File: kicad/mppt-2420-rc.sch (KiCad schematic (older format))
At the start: 10 parts, among them J1 MKDS 5/ 2-9,5, J2 MKDS 5/ 2-9,5, J5 Phoenix Contact MC 1,5

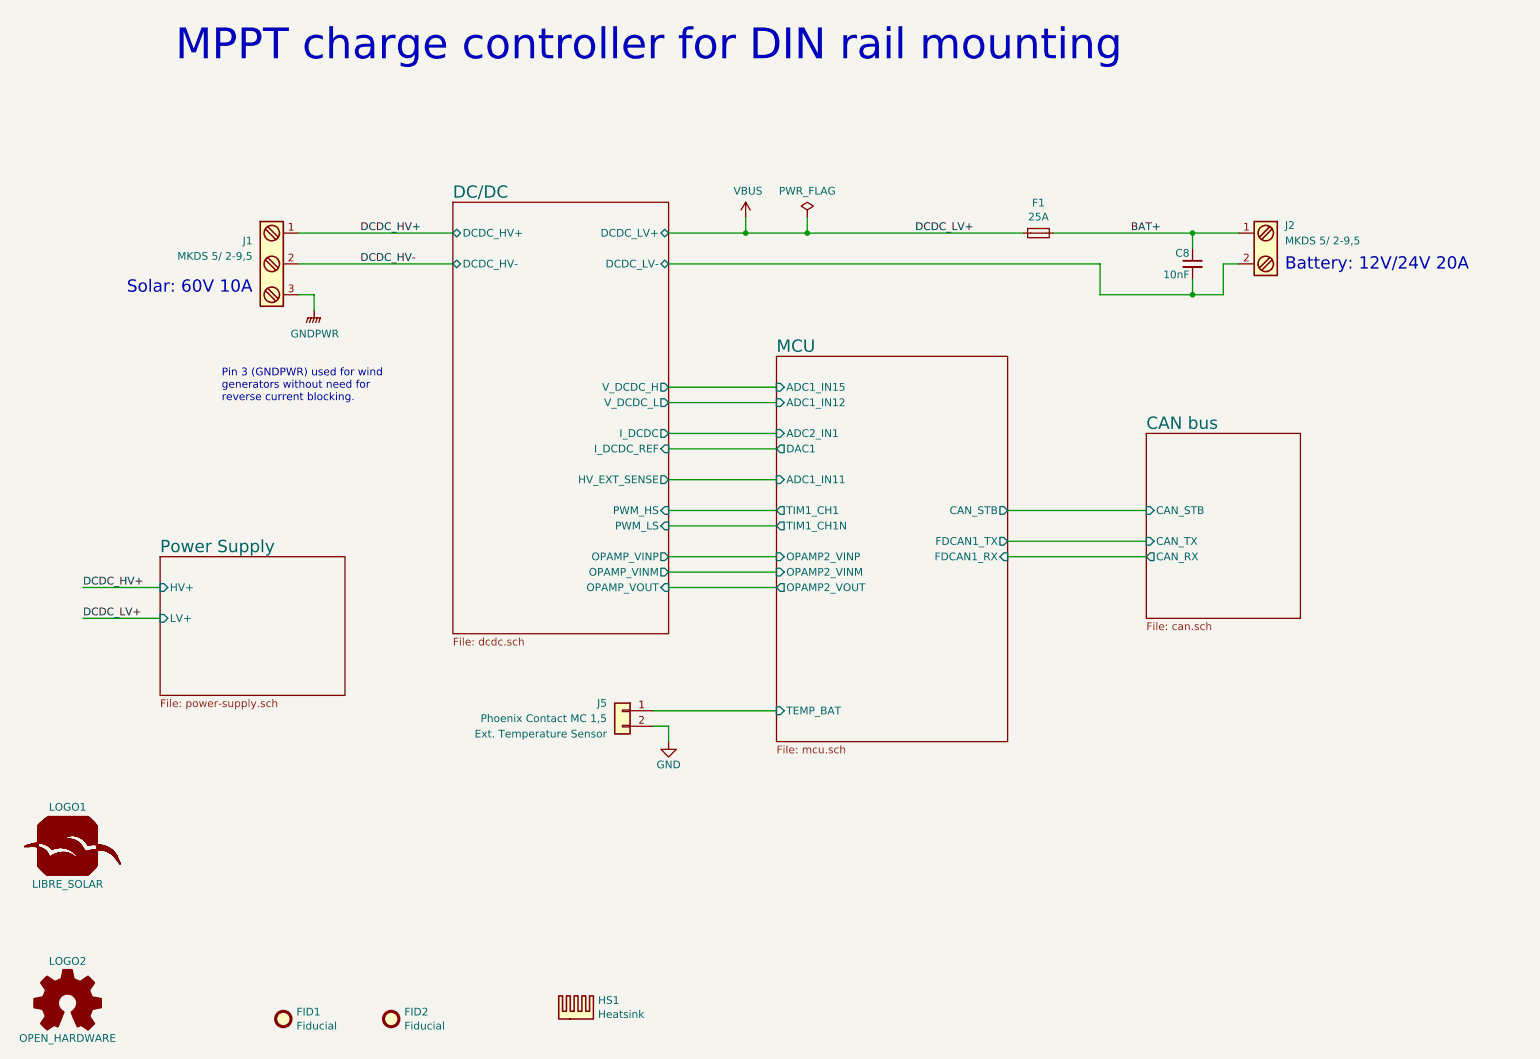
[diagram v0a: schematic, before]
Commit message: Fix errors after first prototype build-up
- Collision of capacitors with MOSFET clamps
- BOOT0 pin tied to GND
- Assignment of a few previously unasigned passives
- Add optional debug serial connector
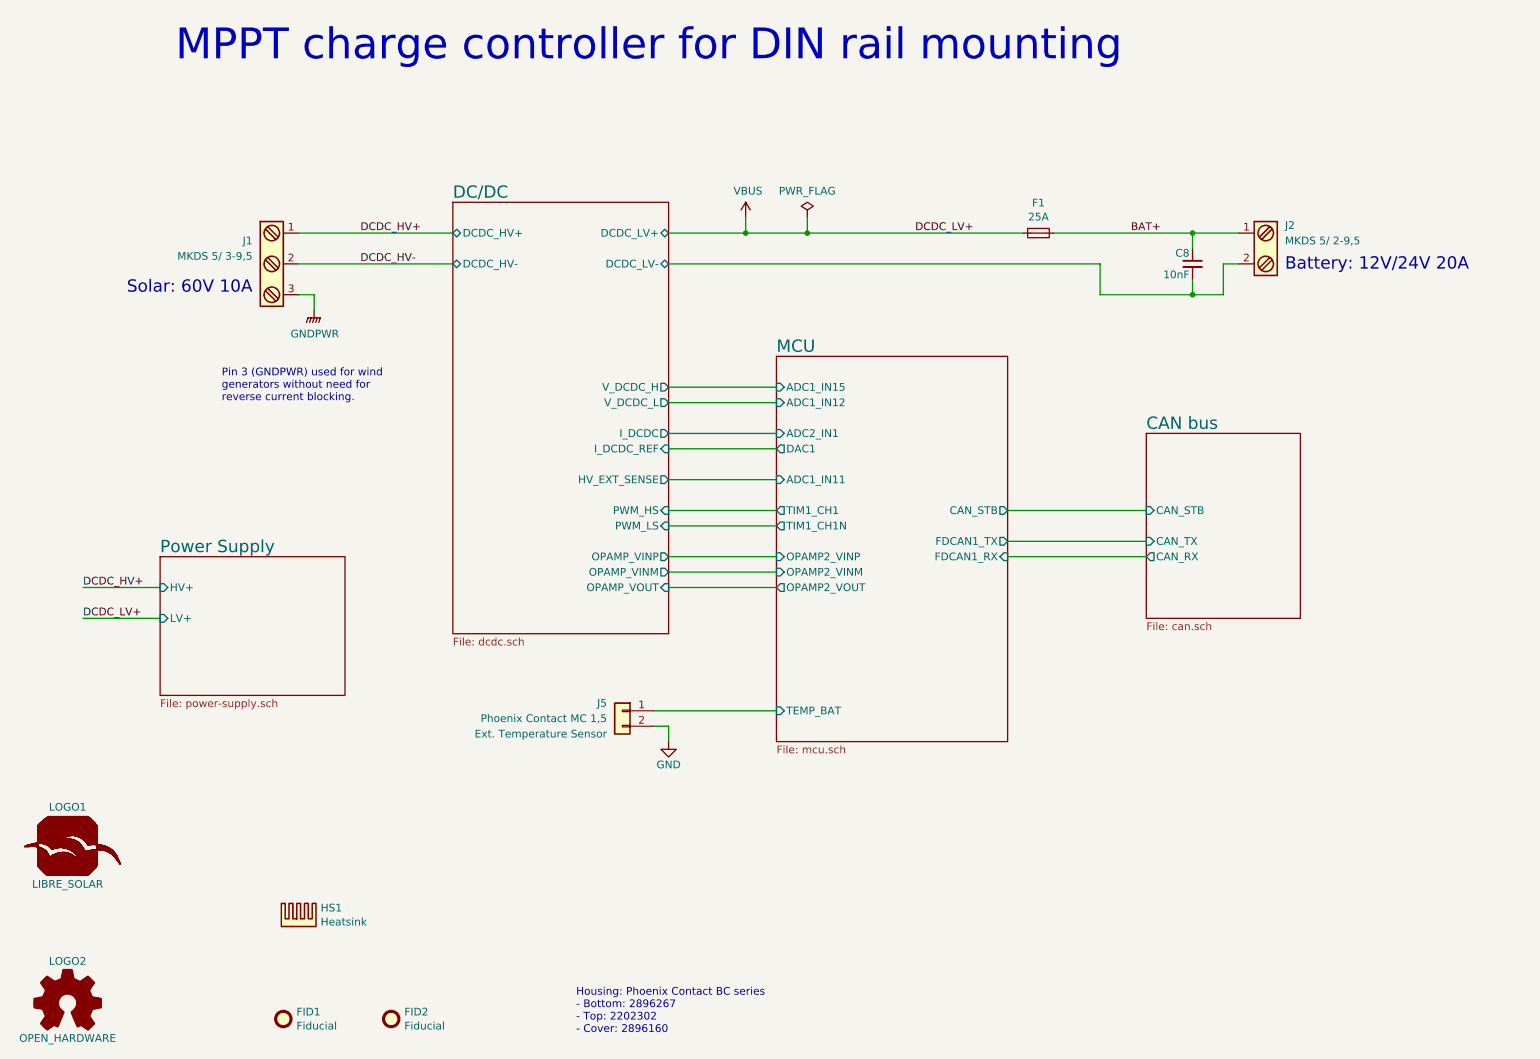
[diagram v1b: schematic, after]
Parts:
- HS1: Manufacturer (none) -> Fischer Elektronik; PartNumber (none) -> SK573-37,5
- J1: value MKDS 5/ 2-9,5 -> MKDS 5/ 3-9,5; Manufacturer (none) -> Phoenix Contact; PartNumber (none) -> 1714984
- J2: Manufacturer (none) -> Phoenix Contact; PartNumber (none) -> 1714971
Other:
- note added: "Housing: Phoenix Contact BC series\n- Bottom: 2896267\n- Top: 2202302\n- Cover: 2896160"
- moved on the sheet: HS1
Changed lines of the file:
@@
 Sheet 1 5
 Title "MPPT 2420 RC"
-Date "2020-02-20"
-Rev "0.1"
+Date "2020-05-30"
+Rev "0.1.1"
 Comp "Libre Solar Technologies GmbH"
 Comment1 "Author: Martin Jäger"
@@
 AR Path="/5CC2E802" Ref="J1"  Part="1"
 F 0 "J1" H 2600 2550 50  0000 R CNN
-F 1 "MKDS 5/ 2-9,5" H 2600 2450 50  0000 R CNN
+F 1 "MKDS 5/ 3-9,5" H 2600 2450 50  0000 R CNN
 F 2 "LibreSolar:Phoenix_Contact_MKDS_5-3-9,5" H 2700 2175 50  0001 C CNN
 F 3 "" H 2675 2400 50  0001 C CNN
+F 4 "Phoenix Contact" H 2700 2400 50  0001 C CNN "Manufacturer"
+F 5 "1714984" H 2700 2400 50  0001 C CNN "PartNumber"
 	1    2700 2400
 	1    0    0    -1
@@
 F 2 "LibreSolar:Phoenix_Contact_MKDS_5-2-9,5" H 9200 2075 50  0001 C CNN
 F 3 "" H 9175 2300 50  0001 C CNN
+F 4 "Phoenix Contact" H 9200 2300 50  0001 C CNN "Manufacturer"
+F 5 "1714971" H 9200 2300 50  0001 C CNN "PartNumber"
 	1    9200 2300
 	-1   0    0    -1
@@
 L Mechanical:Heatsink HS1
 U 1 1 5E1B0EED
-P 4700 7300
-F 0 "HS1" H 4842 7421 50  0000 L CNN
-F 1 "Heatsink" H 4842 7330 50  0000 L CNN
-F 2 "LibreSolar:Fischer_Elektronik_SK573_37,5" H 4712 7300 50  0001 C CNN
-F 3 "~" H 4712 7300 50  0001 C CNN
-	1    4700 7300
+P 2900 6700
+F 0 "HS1" H 3042 6821 50  0000 L CNN
+F 1 "Heatsink" H 3042 6730 50  0000 L CNN
+F 2 "LibreSolar:Fischer_Elektronik_SK573_37,5" H 2912 6700 50  0001 C CNN
+F 3 "~" H 2912 6700 50  0001 C CNN
+F 4 "Fischer Elektronik" H 2900 6700 50  0001 C CNN "Manufacturer"
+F 5 "SK573-37,5" H 2900 6700 50  0001 C CNN "PartNumber"
+	1    2900 6700
 	1    0    0    -1
 $EndComp
@@
 Text Notes 2400 3300 0    50   ~ 0
 Pin 3 (GNDPWR) used for wind\ngenerators without need for \nreverse current blocking.
+Text Notes 4700 7400 0    50   ~ 0
+Housing: Phoenix Contact BC series\n- Bottom: 2896267\n- Top: 2202302\n- Cover: 2896160
 $EndSCHEMATC

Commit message: Fix some references and part numbers
See issues #3, #5, #7, #8 and #9.
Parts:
- added XF1: ATO blade fuse, LibreSolar:Keystone-Fuse-3557-2, symbol LibreSolar:Fuse_Holder
- C8: Manufacturer (none) -> Murata; PartNumber (none) -> GCM188R72A103KA37D; Remarks 50V, X7R -> 100V, X7R
- F1: footprint LibreSolar:Keystone-Fuse-3557-2 -> LibreSolar:NULL; symbol LibreSolar:Fuse -> LibreSolar:Fuse_PlugIn; Manufacturer (none) -> Littelfuse; PartNumber (none) -> 0287025.PXCN
- HS1: Remarks (none) -> 3x MOSFET clips THFU 2 and thermal interface material needed
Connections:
- net BAT+: now also XF1.2; no longer F1.2
- net VBUS: now also XF1.1; no longer F1.1
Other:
- note added: "10k NTC thermistor\n\nMatching connector: \nPhoenix Contact 1745894"
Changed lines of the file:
@@
 F 2 "LibreSolar:C_0603_1608" H 8700 2400 50  0001 C CNN
 F 3 "" H 8700 2400 50  0000 C CNN
-F 4 "" H 6600 650 50  0001 C CNN "Manufacturer"
-F 5 "" H 6600 650 50  0001 C CNN "PartNumber"
-F 6 "50V, X7R" H 6100 300 60  0001 C CNN "Remarks"
+F 4 "Murata" H 6600 650 50  0001 C CNN "Manufacturer"
+F 5 "GCM188R72A103KA37D" H 6600 650 50  0001 C CNN "PartNumber"
+F 6 "100V, X7R" H 6100 300 60  0001 C CNN "Remarks"
 	1    8700 2400
 	-1   0    0    -1
@@
 	9000 2200 8700 2200
 $Comp
-L LibreSolar:Fuse F?
+L LibreSolar:Fuse_PlugIn F?
 U 1 1 5DADB2CD
-P 7700 2200
+P 7700 2100
 AR Path="/5C5B93EE/5DADB2CD" Ref="F?"  Part="1"
 AR Path="/5DADB2CD" Ref="F1"  Part="1"
-F 0 "F1" H 7700 2396 50  0000 C CNN
-F 1 "25A" H 7700 2305 50  0000 C CNN
-F 2 "LibreSolar:Keystone-Fuse-3557-2" H 7700 2200 50  0001 C CNN
-F 3 "" H 7700 2200 50  0000 C CNN
-	1    7700 2200
-	1    0    0    -1
-$EndComp
-Wire Wire Line
-	7800 2200 8700 2200
+F 0 "F1" H 7550 2200 50  0000 C CNN
+F 1 "25A" H 7850 2200 50  0000 C CNN
+F 2 "LibreSolar:NULL" H 7700 2100 50  0001 C CNN
+F 3 "" H 7700 2100 50  0001 C CNN
+F 4 "Littelfuse" H 7700 2100 50  0001 C CNN "Manufacturer"
+F 5 "0287025.PXCN" H 7700 2100 50  0001 C CNN "PartNumber"
+F 6 "" H 7700 2100 50  0001 C CNN "Config"
+	1    7700 2100
+	1    0    0    -1
+$EndComp
 Wire Wire Line
 	5300 2200 5800 2200
@@
 F 4 "Fischer Elektronik" H 2900 6700 50  0001 C CNN "Manufacturer"
 F 5 "SK573-37,5" H 2900 6700 50  0001 C CNN "PartNumber"
+F 6 "3x MOSFET clips THFU 2 and thermal interface material needed" H 2900 6700 50  0001 C CNN "Remarks"
 	1    2900 6700
 	1    0    0    -1
@@
 	2900 2200 3900 2200
 Wire Wire Line
-	6200 2200 7600 2200
+	6200 2200 7500 2200
 Wire Wire Line
 	2900 2600 3000 2600
@@
 	3000 2600 3000 2700
 Wire Wire Line
-	5300 2400 8100 2400
-Wire Wire Line
-	8100 2400 8100 2600
-Wire Wire Line
-	8100 2600 8700 2600
+	5300 2400 7200 2400
+Wire Wire Line
+	7200 2400 7200 2600
+Wire Wire Line
+	7200 2600 8700 2600
 Connection ~ 8700 2600
 $Sheet
@@
 Text Notes 4700 7400 0    50   ~ 0
 Housing: Phoenix Contact BC series\n- Bottom: 2896267\n- Top: 2202302\n- Cover: 2896160
+Text Notes 4000 5900 0    50   ~ 0
+10k NTC thermistor\n\nMatching connector: \nPhoenix Contact 1745894
+$Comp
+L LibreSolar:Fuse_Holder XF1
+U 1 1 5F259FDF
+P 7700 2200
+F 0 "XF1" H 7700 2200 50  0000 C CNN
+F 1 "ATO blade fuse" H 7700 2100 50  0000 C CNN
+F 2 "LibreSolar:Keystone-Fuse-3557-2" H 7700 2200 50  0001 C CNN
+F 3 "" H 7700 2200 50  0001 C CNN
+	1    7700 2200
+	1    0    0    -1
+$EndComp
+Wire Wire Line
+	7900 2200 8700 2200
 $EndSCHEMATC

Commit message: Clean up BOM and add build folder for generated files
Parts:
- J2: symbol Project:Screw_Terminal_1x02 -> LibreSolar:Screw_Terminal_1x02_Large
- XF1: Manufacturer (none) -> Keystone; PartNumber (none) -> 3557-2
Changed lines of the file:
@@
 DCDC_HV+
 $Comp
-L Project:Screw_Terminal_1x02 J?
+L LibreSolar:Screw_Terminal_1x02_Large J?
 U 1 1 5CE7E6AC
 P 9200 2300
@@
 F 2 "LibreSolar:Keystone-Fuse-3557-2" H 7700 2200 50  0001 C CNN
 F 3 "" H 7700 2200 50  0001 C CNN
+F 4 "Keystone" H 7700 2200 50  0001 C CNN "Manufacturer"
+F 5 "3557-2" H 7700 2200 50  0001 C CNN "PartNumber"
 	1    7700 2200
 	1    0    0    -1
